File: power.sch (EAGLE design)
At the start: 21 parts

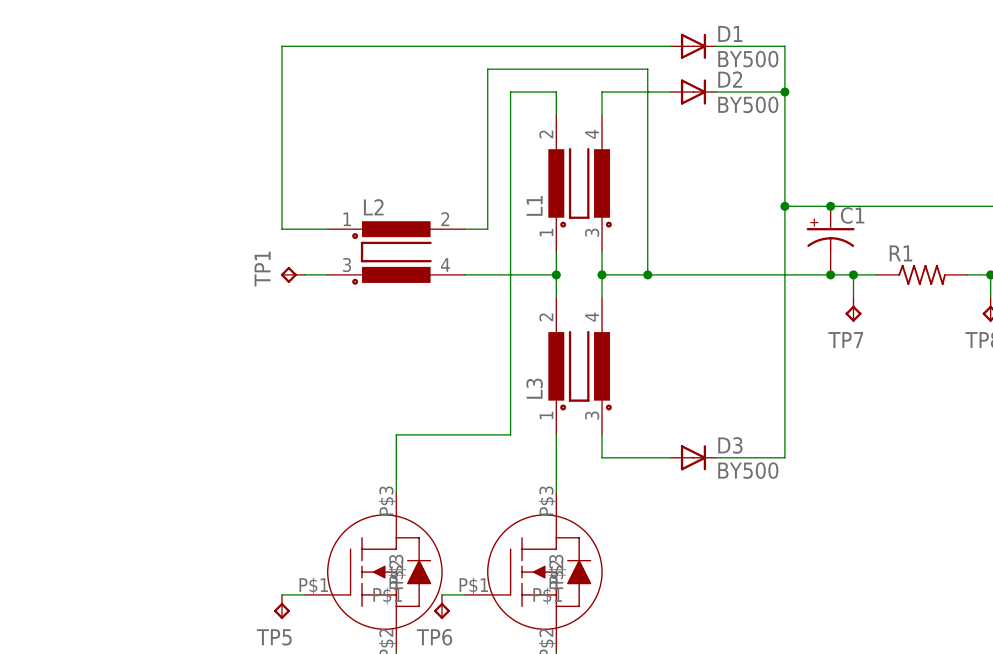
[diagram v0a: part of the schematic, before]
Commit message: Transformer footprints and really awful looking board routing
Pretty sure at least one of the transformers is wired in the wrong way
too
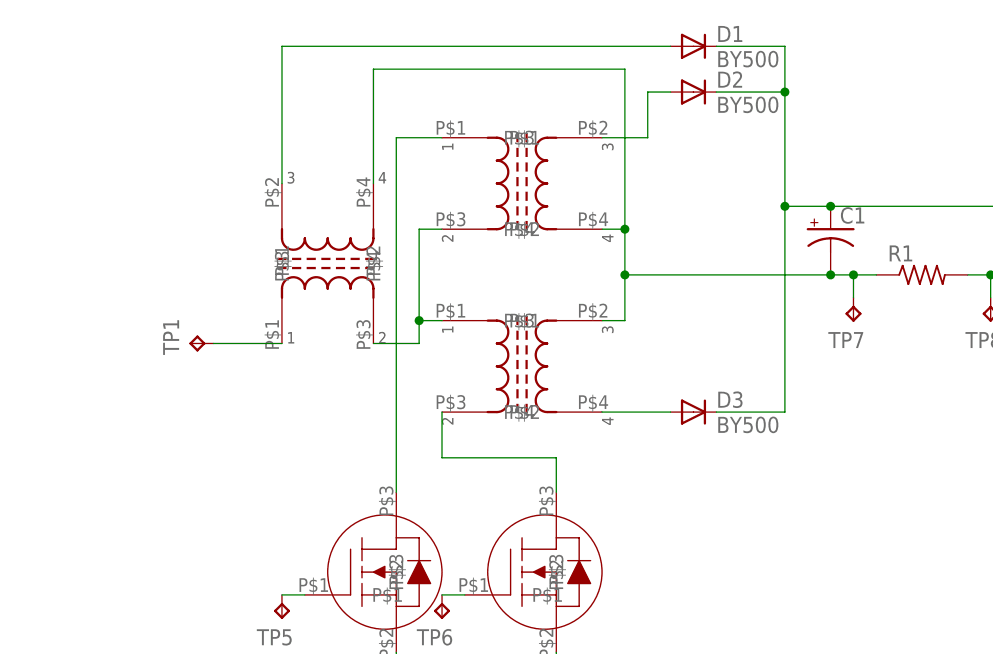
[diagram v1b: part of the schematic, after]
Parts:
- removed L1, L3: (no value), inductor-nkl:R1405UB2
- removed L2: (no value), inductor-nkl:R1405UB1
- added U$3: PLH10AN2211R5P2B, chokes:PLH10AN2211R5P2B
- added U$4, U$5: TLF14CBH3321R0K1, chokes:TLF14CBH3321R0K1
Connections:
- removed net N$7: D2.A, L1.4
- new net N$15: U$1.P$2, U$5.P$1
- net N$1: now also U$3.P$3; no longer L2.1
- net N$2: now also D2.A, U$5.P$3; no longer L1.1, L2.4, L3.2
- net N$3: now also U$3.P$1; no longer L2.3
- net N$4: now also U$3.P$4, U$4.P$3, U$5.P$4; no longer L1.3, L2.2, L3.4
- net N$5: now also U$4.P$2; no longer L3.1
- net N$6: now also U$3.P$2, U$4.P$1, U$5.P$2; no longer L1.2, U$1.P$2
- net N$9: now also U$4.P$4; no longer L3.3
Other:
- moved on the sheet: D3, TP1
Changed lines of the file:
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@@
 <?xml version="1.0" encoding="utf-8"?>
 <!DOCTYPE eagle SYSTEM "eagle.dtd">
-<eagle version="6.5.0">
+<eagle version="6.5.1">
 <drawing>
 <settings>
@@
 <part name="TP7" library="testpad" deviceset="TP" device="PAD1-13Y"/>
 <part name="TP8" library="testpad" deviceset="TP" device="PAD1-13Y"/>
-<part name="L1" library="inductor-nkl" deviceset="R1405U" device="B2"/>
-<part name="L2" library="inductor-nkl" deviceset="R1405U" device="B1"/>
-<part name="L3" library="inductor-nkl" deviceset="R1405U" device="B2"/>
 <part name="D1" library="diode" deviceset="BY500" device=""/>
 <part name="D2" library="diode" deviceset="BY500" device=""/>
@@
 <part name="TP10" library="testpad" deviceset="TP" device="PAD1-13Y"/>
 <part name="R2" library="rcl" deviceset="R-US_" device="R0603"/>
+<part name="U$3" library="chokes" deviceset="PLH10AN2211R5P2B" device=""/>
+<part name="U$4" library="chokes" deviceset="TLF14CBH3321R0K1" device=""/>
+<part name="U$5" library="chokes" deviceset="TLF14CBH3321R0K1" device=""/>
 </parts>
 <sheets>
@@
 </plain>
 <instances>
-<instance part="TP1" gate="G$1" x="12.7" y="50.8" rot="R90"/>
+<instance part="TP1" gate="G$1" x="2.54" y="43.18" rot="R90"/>
 <instance part="TP2" gate="G$1" x="-12.7" y="5.08" rot="R90"/>
 <instance part="TP3" gate="G$1" x="96.52" y="58.42" rot="R270"/>
@@
 <instance part="TP7" gate="G$1" x="76.2" y="45.72" rot="R180"/>
 <instance part="TP8" gate="G$1" x="91.44" y="45.72" rot="R180"/>
-<instance part="L1" gate="G$1" x="45.72" y="60.96" rot="R90"/>
-<instance part="L2" gate="G$1" x="25.4" y="53.34"/>
-<instance part="L3" gate="G$1" x="45.72" y="40.64" rot="R90"/>
 <instance part="D1" gate="1" x="58.42" y="76.2"/>
 <instance part="D2" gate="1" x="58.42" y="71.12"/>
-<instance part="D3" gate="1" x="58.42" y="30.48"/>
+<instance part="D3" gate="1" x="58.42" y="35.56"/>
 <instance part="C1" gate="G$1" x="73.66" y="55.88"/>
 <instance part="U$1" gate="G$1" x="24.13" y="17.78"/>
@@
 <instance part="TP10" gate="G$1" x="10.16" y="0" rot="R180"/>
 <instance part="R2" gate="G$1" x="2.54" y="5.08"/>
+<instance part="U$3" gate="G$1" x="17.78" y="53.34"/>
+<instance part="U$4" gate="G$1" x="40.64" y="40.64" rot="R270"/>
+<instance part="U$5" gate="G$1" x="40.64" y="60.96" rot="R270"/>
 </instances>
 <busses>
 </busses>
 <nets>
-<net name="N$1" class="0">
-<segment>
-<pinref part="L2" gate="G$1" pin="1"/>
-<wire x1="12.7" y1="55.88" x2="17.78" y2="55.88" width="0.1524" layer="91"/>
-<wire x1="12.7" y1="55.88" x2="12.7" y2="76.2" width="0.1524" layer="91"/>
-<wire x1="12.7" y1="76.2" x2="55.88" y2="76.2" width="0.1524" layer="91"/>
-<pinref part="D1" gate="1" pin="A"/>
-</segment>
-</net>
 <net name="N$3" class="0">
 <segment>
-<pinref part="L2" gate="G$1" pin="3"/>
 <pinref part="TP1" gate="G$1" pin="TP"/>
-<wire x1="17.78" y1="50.8" x2="15.24" y2="50.8" width="0.1524" layer="91"/>
+<wire x1="12.7" y1="43.18" x2="5.08" y2="43.18" width="0.1524" layer="91"/>
+<pinref part="U$3" gate="G$1" pin="P$1"/>
 </segment>
 </net>
 <net name="N$4" class="0">
 <segment>
-<pinref part="L3" gate="G$1" pin="4"/>
-<pinref part="L1" gate="G$1" pin="3"/>
-<wire x1="48.26" y1="48.26" x2="48.26" y2="50.8" width="0.1524" layer="91"/>
-<pinref part="L2" gate="G$1" pin="2"/>
-<wire x1="48.26" y1="50.8" x2="48.26" y2="53.34" width="0.1524" layer="91"/>
-<wire x1="33.02" y1="55.88" x2="35.56" y2="55.88" width="0.1524" layer="91"/>
-<wire x1="35.56" y1="55.88" x2="35.56" y2="73.66" width="0.1524" layer="91"/>
-<wire x1="35.56" y1="73.66" x2="53.34" y2="73.66" width="0.1524" layer="91"/>
-<wire x1="53.34" y1="73.66" x2="53.34" y2="50.8" width="0.1524" layer="91"/>
-<wire x1="53.34" y1="50.8" x2="48.26" y2="50.8" width="0.1524" layer="91"/>
-<junction x="48.26" y="50.8"/>
-<wire x1="53.34" y1="50.8" x2="73.66" y2="50.8" width="0.1524" layer="91"/>
-<junction x="53.34" y="50.8"/>
+<wire x1="22.86" y1="73.66" x2="50.8" y2="73.66" width="0.1524" layer="91"/>
+<wire x1="50.8" y1="73.66" x2="50.8" y2="55.88" width="0.1524" layer="91"/>
+<wire x1="50.8" y1="55.88" x2="50.8" y2="50.8" width="0.1524" layer="91"/>
+<wire x1="50.8" y1="50.8" x2="73.66" y2="50.8" width="0.1524" layer="91"/>
 <pinref part="C1" gate="G$1" pin="-"/>
 <wire x1="73.66" y1="50.8" x2="76.2" y2="50.8" width="0.1524" layer="91"/>
@@
 <wire x1="76.2" y1="50.8" x2="76.2" y2="48.26" width="0.1524" layer="91"/>
 <junction x="76.2" y="50.8"/>
-</segment>
-</net>
-<net name="N$6" class="0">
-<segment>
-<pinref part="L1" gate="G$1" pin="2"/>
-<wire x1="43.18" y1="68.58" x2="43.18" y2="71.12" width="0.1524" layer="91"/>
-<wire x1="43.18" y1="71.12" x2="38.1" y2="71.12" width="0.1524" layer="91"/>
-<wire x1="38.1" y1="71.12" x2="38.1" y2="33.02" width="0.1524" layer="91"/>
-<pinref part="U$1" gate="G$1" pin="P$2"/>
-<wire x1="25.4" y1="26.67" x2="25.4" y2="33.02" width="0.1524" layer="91"/>
-<wire x1="25.4" y1="33.02" x2="38.1" y2="33.02" width="0.1524" layer="91"/>
-</segment>
-</net>
-<net name="N$7" class="0">
-<segment>
-<pinref part="L1" gate="G$1" pin="4"/>
-<pinref part="D2" gate="1" pin="A"/>
-<wire x1="48.26" y1="68.58" x2="48.26" y2="71.12" width="0.1524" layer="91"/>
-<wire x1="48.26" y1="71.12" x2="55.88" y2="71.12" width="0.1524" layer="91"/>
+<pinref part="U$3" gate="G$1" pin="P$4"/>
+<wire x1="22.86" y1="73.66" x2="22.86" y2="60.96" width="0.1524" layer="91"/>
+<pinref part="U$5" gate="G$1" pin="P$4"/>
+<wire x1="48.26" y1="55.88" x2="50.8" y2="55.88" width="0.1524" layer="91"/>
+<junction x="50.8" y="55.88"/>
+<pinref part="U$4" gate="G$1" pin="P$3"/>
+<wire x1="48.26" y1="45.72" x2="50.8" y2="45.72" width="0.1524" layer="91"/>
+<wire x1="50.8" y1="45.72" x2="50.8" y2="50.8" width="0.1524" layer="91"/>
+<junction x="50.8" y="50.8"/>
 </segment>
 </net>
@@
 <junction x="73.66" y="58.42"/>
 <pinref part="D3" gate="1" pin="C"/>
-<wire x1="60.96" y1="30.48" x2="68.58" y2="30.48" width="0.1524" layer="91"/>
-<wire x1="68.58" y1="30.48" x2="68.58" y2="58.42" width="0.1524" layer="91"/>
+<wire x1="60.96" y1="35.56" x2="68.58" y2="35.56" width="0.1524" layer="91"/>
+<wire x1="68.58" y1="35.56" x2="68.58" y2="58.42" width="0.1524" layer="91"/>
 <junction x="68.58" y="58.42"/>
 </segment>
@@
 <net name="N$9" class="0">
 <segment>
-<pinref part="L3" gate="G$1" pin="3"/>
 <pinref part="D3" gate="1" pin="A"/>
-<wire x1="48.26" y1="33.02" x2="48.26" y2="30.48" width="0.1524" layer="91"/>
-<wire x1="48.26" y1="30.48" x2="55.88" y2="30.48" width="0.1524" layer="91"/>
+<pinref part="U$4" gate="G$1" pin="P$4"/>
+<wire x1="48.26" y1="35.56" x2="55.88" y2="35.56" width="0.1524" layer="91"/>
 </segment>
 </net>
@@
 <segment>
 <pinref part="U$2" gate="G$1" pin="P$2"/>
-<pinref part="L3" gate="G$1" pin="1"/>
-<wire x1="43.18" y1="26.67" x2="43.18" y2="33.02" width="0.1524" layer="91"/>
+<wire x1="43.18" y1="26.67" x2="43.18" y2="30.48" width="0.1524" layer="91"/>
+<pinref part="U$4" gate="G$1" pin="P$2"/>
+<wire x1="30.48" y1="35.56" x2="30.48" y2="30.48" width="0.1524" layer="91"/>
+<wire x1="30.48" y1="30.48" x2="43.18" y2="30.48" width="0.1524" layer="91"/>
 </segment>
 </net>
@@
 </segment>
 </net>
+<net name="N$1" class="0">
+<segment>
+<pinref part="D1" gate="1" pin="A"/>
+<pinref part="U$3" gate="G$1" pin="P$3"/>
+<wire x1="55.88" y1="76.2" x2="12.7" y2="76.2" width="0.1524" layer="91"/>
+<wire x1="12.7" y1="76.2" x2="12.7" y2="60.96" width="0.1524" layer="91"/>
+</segment>
+</net>
 <net name="N$2" class="0">
 <segment>
-<pinref part="L3" gate="G$1" pin="2"/>
-<pinref part="L1" gate="G$1" pin="1"/>
-<wire x1="43.18" y1="53.34" x2="43.18" y2="50.8" width="0.1524" layer="91"/>
-<pinref part="L2" gate="G$1" pin="4"/>
-<wire x1="43.18" y1="50.8" x2="43.18" y2="48.26" width="0.1524" layer="91"/>
-<wire x1="33.02" y1="50.8" x2="43.18" y2="50.8" width="0.1524" layer="91"/>
-<junction x="43.18" y="50.8"/>
-</segment>
-</net>
+<pinref part="D2" gate="1" pin="A"/>
+<wire x1="55.88" y1="71.12" x2="53.34" y2="71.12" width="0.1524" layer="91"/>
+<wire x1="53.34" y1="71.12" x2="53.34" y2="66.04" width="0.1524" layer="91"/>
+<pinref part="U$5" gate="G$1" pin="P$3"/>
+<wire x1="53.34" y1="66.04" x2="48.26" y2="66.04" width="0.1524" layer="91"/>
+</segment>
+</net>
+<net name="N$15" class="0">
+<segment>
+<pinref part="U$5" gate="G$1" pin="P$1"/>
+<wire x1="30.48" y1="66.04" x2="25.4" y2="66.04" width="0.1524" layer="91"/>
+<pinref part="U$1" gate="G$1" pin="P$2"/>
+<wire x1="25.4" y1="66.04" x2="25.4" y2="26.67" width="0.1524" layer="91"/>
+</segment>
+</net>
+<net name="N$6" class="0">
+<segment>
+<pinref part="U$3" gate="G$1" pin="P$2"/>
+<wire x1="22.86" y1="43.18" x2="27.94" y2="43.18" width="0.1524" layer="91"/>
+<pinref part="U$5" gate="G$1" pin="P$2"/>
+<wire x1="30.48" y1="55.88" x2="27.94" y2="55.88" width="0.1524" layer="91"/>
+<wire x1="27.94" y1="55.88" x2="27.94" y2="45.72" width="0.1524" layer="91"/>
+<pinref part="U$4" gate="G$1" pin="P$1"/>
+<wire x1="27.94" y1="45.72" x2="27.94" y2="43.18" width="0.1524" layer="91"/>
+<wire x1="27.94" y1="45.72" x2="30.48" y2="45.72" width="0.1524" layer="91"/>
+<junction x="27.94" y="45.72"/>
+</segment>
+</net>

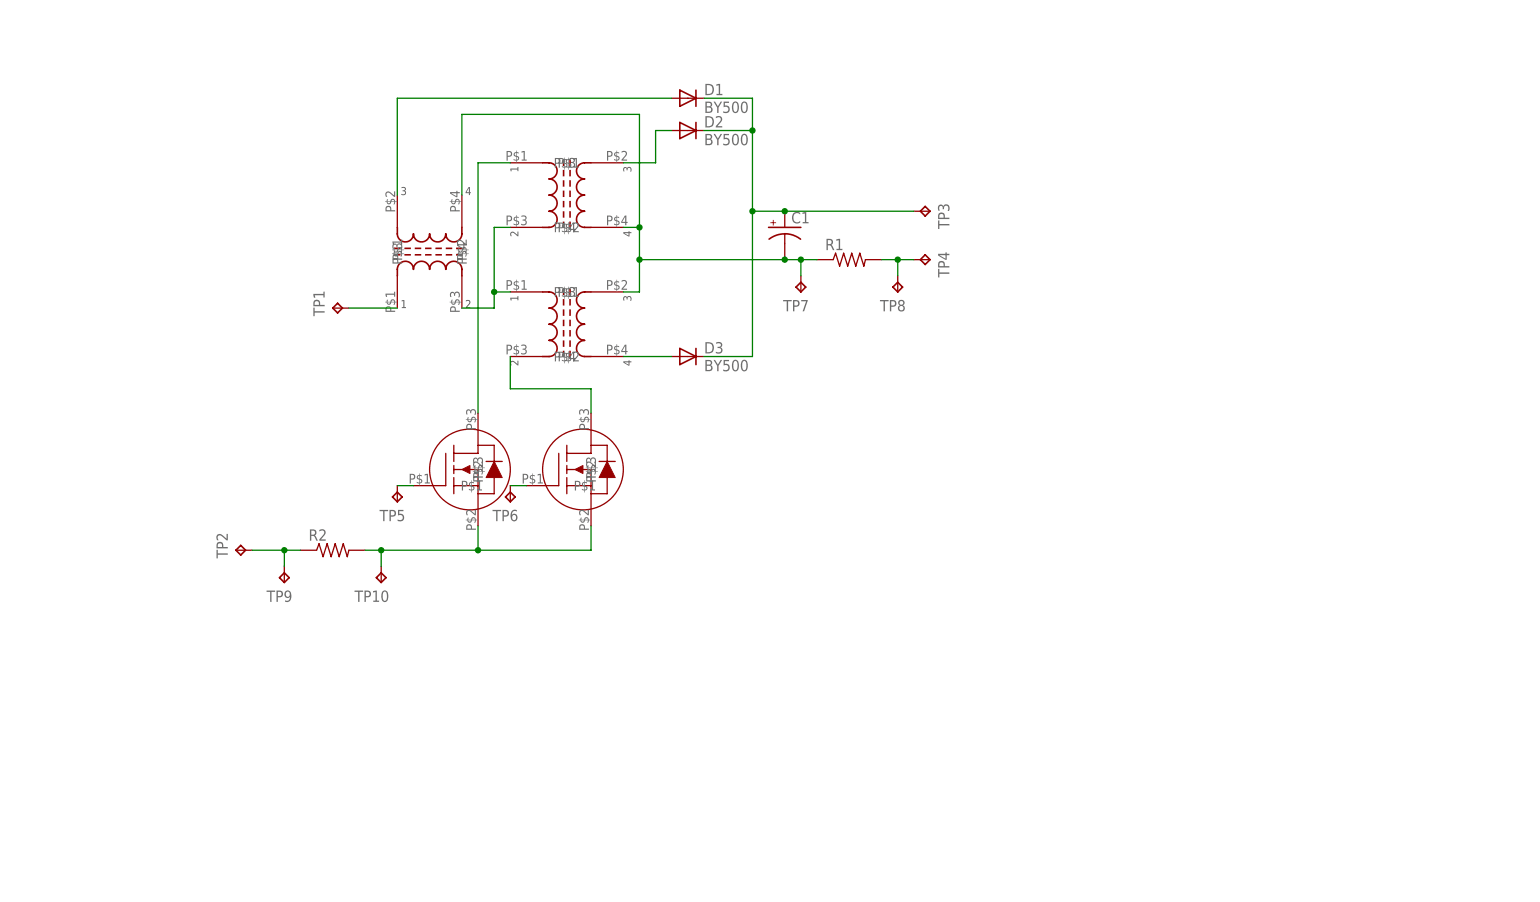
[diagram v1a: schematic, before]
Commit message: proposed beaglebone connections and resistor dividers
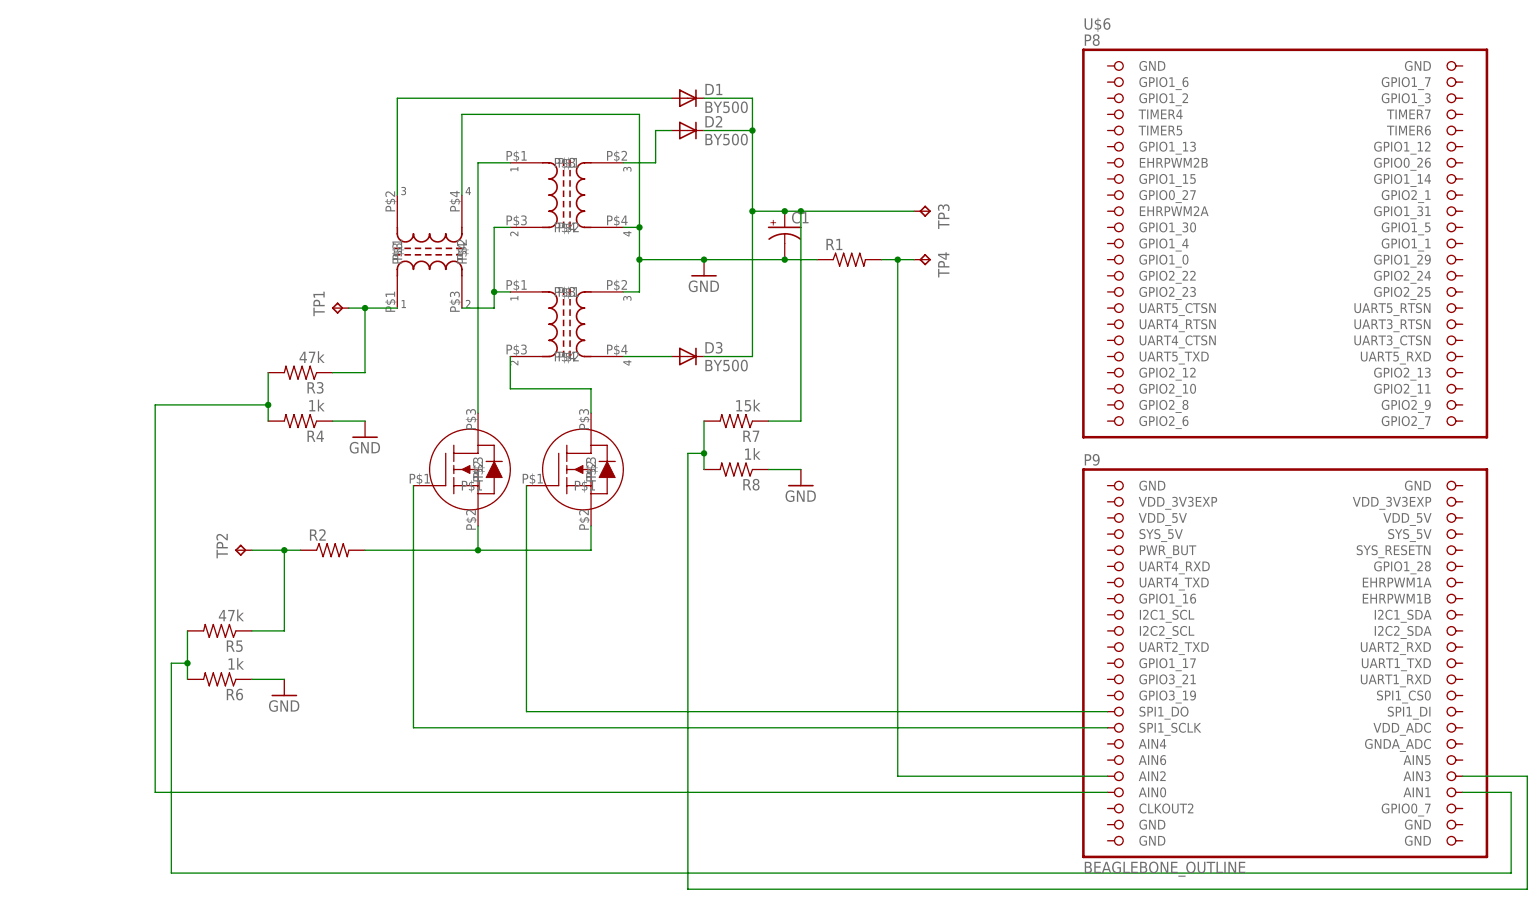
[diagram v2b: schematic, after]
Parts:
- removed TP10, TP5, TP6, TP7, TP8, TP9: TPPAD1-13Y, testpad:TPPAD1-13Y
- added R3, R5: 47k, rcl:R-US_R0603
- added R4, R6, R8: 1k, rcl:R-US_R0603
- added R7: 15k, rcl:R-US_R0603
- added U$6: BEAGLEBONE_OUTLINE, adafruit:BEAGLEBONE_OUTLINE
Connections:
- removed net N$8: C1.+, D1.C, D2.C, D3.C, TP3.TP
- new net GND: C1.-, R1.1, R4.1, R6.1, R8.1, U$3.P$4, U$4.P$3, U$5.P$4
- new net N$16: R2.1, R5.1, TP2.TP
- new net N$17: R5.2, R6.2, U$6.AIN1
- new net N$7: C1.+, D1.C, D2.C, D3.C, R7.1, TP3.TP
- net N$10: now also R7.2, R8.2, U$6.AIN3; no longer R2.1, TP2.TP, TP9.TP
- net N$11: no longer TP10.TP
- net N$12: now also U$6.SPI1_SCLK; no longer TP5.TP
- net N$13: now also U$6.SPI1_DO; no longer TP6.TP
- net N$14: now also U$6.AIN2; no longer TP8.TP
- net N$3: now also R3.1
- net N$4: now also R3.2, R4.2, U$6.AIN0; no longer C1.-, R1.1, TP7.TP, U$3.P$4, U$4.P$3, U$5.P$4
